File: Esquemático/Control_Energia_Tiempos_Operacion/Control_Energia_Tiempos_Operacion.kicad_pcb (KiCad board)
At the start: 2 copper layers, 100 x 100 mm, 14 parts, among them J1 Conn_01x02_Socket, Q1 BC548, U1 ATmega328P-P, U2 DS3231M, Y1 16MHz

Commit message: Corrección PCB
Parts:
- moved C1 1.52 mm to (146.5, 84.5)
- moved C2 1.52 mm to (141.4, 84.5)
- moved Y1 1.52 mm to (141.6, 91.5)
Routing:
- net Net-(DS1-VO): track 54.5 -> 56.2 mm
- net Net-(U1-XTAL2/PB7): track 16.9 -> 17.7 mm
- net Net-(U1-XTAL1/PB6): track 17.9 -> 17.2 mm
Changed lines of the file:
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@@
   )
   (footprint "Capacitor_THT:C_Disc_D5.0mm_W2.5mm_P2.50mm" (layer "F.Cu")
-    (at 148 84.5 90)
+    (at 146.48 84.5 90)
     (descr "C, Disc series, Radial, pin pitch=2.50mm, , diameter*width=5*2.5mm^2, Capacitor, http://cdn-reichelt.de/documents/datenblatt/B300/DS_KERKO_TC.pdf")
     (tags "C Disc series Radial pin pitch 2.50mm  diameter 5mm width 2.5mm Capacitor")
@@
   )
   (footprint "Capacitor_THT:C_Disc_D5.0mm_W2.5mm_P2.50mm" (layer "F.Cu")
-    (at 142.95 84.5 90)
+    (at 141.43 84.5 90)
     (descr "C, Disc series, Radial, pin pitch=2.50mm, , diameter*width=5*2.5mm^2, Capacitor, http://cdn-reichelt.de/documents/datenblatt/B300/DS_KERKO_TC.pdf")
     (tags "C Disc series Radial pin pitch 2.50mm  diameter 5mm width 2.5mm Capacitor")
@@
   )
   (footprint "Crystal:Crystal_HC49-4H_Vertical" (layer "F.Cu")
-    (at 143.07 91.5)
+    (at 141.55 91.5)
     (descr "Crystal THT HC-49-4H http://5hertz.com/pdfs/04404_D.pdf")
     (tags "THT crystalHC-49-4H")
@@
     (pad "2" thru_hole roundrect (at 0 0) (size 2 2) (drill 1) (layers "*.Cu" "*.Mask") (roundrect_rratio 0.147059)
       (net 2 "+5V") (pinfunction "VDD") (pintype "power_in"))
-    (pad "3" thru_hole circle (at 0 7.62) (size 2 2) (drill 1) (layers "*.Cu" "*.Mask")
+    (pad "3" thru_hole circle (at 0 5.08) (size 2 2) (drill 1) (layers "*.Cu" "*.Mask")
       (net 3 "Net-(DS1-VO)") (pinfunction "VO") (pintype "input"))
     (pad "4" thru_hole circle (at 2.54 0) (size 2 2) (drill 1) (layers "*.Cu" "*.Mask")
       (net 4 "LCD_RS") (pinfunction "RS") (pintype "input"))
-    (pad "5" thru_hole circle (at 0 5.08) (size 2 2) (drill 1) (layers "*.Cu" "*.Mask")
+    (pad "5" thru_hole circle (at 0 7.62) (size 2 2) (drill 1) (layers "*.Cu" "*.Mask")
       (net 1 "GND") (pinfunction "R/W") (pintype "input"))
     (pad "6" thru_hole circle (at 2.54 2.54) (size 2 2) (drill 1) (layers "*.Cu" "*.Mask")
@@
     (pad "1" thru_hole circle (at 2.54 2.54 180) (size 1.7 1.7) (drill 1) (layers "*.Cu" "*.Mask")
       (net 2 "+5V") (pinfunction "V+") (pintype "power_in"))
-    (pad "2" thru_hole circle (at 2.54 0 180) (size 1.7 1.7) (drill 1) (layers "*.Cu" "*.Mask")
+    (pad "2" thru_hole circle (at 2.54 5.08 180) (size 1.7 1.7) (drill 1) (layers "*.Cu" "*.Mask")
       (net 1 "GND") (pinfunction "GND") (pintype "power_in"))
     (pad "3" thru_hole circle (at 0 2.54 180) (size 1.7 1.7) (drill 1) (layers "*.Cu" "*.Mask")
@@
     (pad "5" thru_hole circle (at 0 5.08 180) (size 1.7 1.7) (drill 1) (layers "*.Cu" "*.Mask")
       (net 11 "SWITCH") (pinfunction "SW") (pintype "output"))
-    (pad "6" thru_hole circle (at 2.54 5.08 180) (size 1.7 1.7) (drill 1) (layers "*.Cu" "*.Mask"))
+    (pad "6" thru_hole circle (at 2.54 0 180) (size 1.7 1.7) (drill 1) (layers "*.Cu" "*.Mask"))
     (model "${KICAD6_3DMODEL_DIR}/Connector_IDC.3dshapes/IDC-Header_2x03_P2.54mm_Vertical.wrl"
       (offset (xyz 0 0 0))
@@
   (via (at 189 136) (size 2.5) (drill 1.25) (layers "F.Cu" "B.Cu") (free) (net 1))
   (via (at 147 121) (size 2.5) (drill 1.25) (layers "F.Cu" "B.Cu") (free) (net 1))
-  (segment (start 124 121) (end 124 129) (width 1) (layer "F.Cu") (net 2))
+  (segment (start 124 121) (end 124 132) (width 1) (layer "F.Cu") (net 2))
   (via (at 124 121) (size 2.5) (drill 1.25) (layers "F.Cu" "B.Cu") (free) (net 2))
-  (via (at 124 129) (size 2.5) (drill 1.25) (layers "F.Cu" "B.Cu") (free) (net 2))
-  (segment (start 129 141) (end 129 138) (width 1.5) (layer "B.Cu") (net 2))
+  (via (at 124 132) (size 2.5) (drill 1.25) (layers "F.Cu" "B.Cu") (free) (net 2))
   (segment (start 102 134) (end 102 106) (width 1.5) (layer "B.Cu") (net 2))
   (segment (start 108.46 106.46) (end 102.46 106.46) (width 1.5) (layer "B.Cu") (net 2))
   (segment (start 190 121) (end 194 121) (width 1) (layer "B.Cu") (net 2))
+  (segment (start 129 138) (end 129 141) (width 1.5) (layer "B.Cu") (net 2))
   (segment (start 102 100) (end 102 90) (width 1.5) (layer "B.Cu") (net 2))
-  (segment (start 129 138) (end 124 133) (width 1.5) (layer "B.Cu") (net 2))
   (segment (start 102.46 106.46) (end 102 106) (width 1.5) (layer "B.Cu") (net 2))
-  (segment (start 124 133) (end 124 129) (width 1.5) (layer "B.Cu") (net 2))
   (segment (start 194 132) (end 194 122) (width 1.5) (layer "B.Cu") (net 2))
   (segment (start 194 122) (end 194 121) (width 1.5) (layer "B.Cu") (net 2))
@@
   (segment (start 129 141) (end 129 147) (width 1.5) (layer "B.Cu") (net 2))
   (segment (start 115 147) (end 102 134) (width 1.5) (layer "B.Cu") (net 2))
+  (segment (start 124 133) (end 129 138) (width 1.5) (layer "B.Cu") (net 2))
   (segment (start 153.08 142) (end 153.08 146.92) (width 1.5) (layer "B.Cu") (net 2))
   (segment (start 139 119) (end 139 120) (width 1) (layer "B.Cu") (net 2))
@@
   (segment (start 153 92) (end 187 92) (width 1.5) (layer "B.Cu") (net 2))
   (segment (start 102 88) (end 102 71) (width 1.5) (layer "B.Cu") (net 2))
-  (segment (start 116 145) (end 104 133) (width 1) (layer "B.Cu") (net 3))
-  (segment (start 104 133) (end 104 114.08) (width 1) (layer "B.Cu") (net 3))
+  (segment (start 124 132) (end 124 133) (width 1.5) (layer "B.Cu") (net 2))
+  (segment (start 105.46 111.54) (end 108.46 111.54) (width 1) (layer "B.Cu") (net 3))
   (segment (start 126.46 141) (end 126.46 144.54) (width 1) (layer "B.Cu") (net 3))
   (segment (start 126.46 144.54) (end 126 145) (width 1) (layer "B.Cu") (net 3))
+  (segment (start 104 133) (end 104 113) (width 1) (layer "B.Cu") (net 3))
   (segment (start 126 145) (end 116 145) (width 1) (layer "B.Cu") (net 3))
-  (segment (start 104 114.08) (end 108.46 114.08) (width 1) (layer "B.Cu") (net 3))
+  (segment (start 104 113) (end 105.46 111.54) (width 1) (layer "B.Cu") (net 3))
+  (segment (start 116 145) (end 104 133) (width 1) (layer "B.Cu") (net 3))
   (segment (start 133.985 103.015) (end 118.985 103.015) (width 0.75) (layer "B.Cu") (net 4))
   (segment (start 118.985 103.015) (end 115.54 106.46) (width 0.75) (layer "B.Cu") (net 4))
@@
   (segment (start 140.1 109.9) (end 140.1 108.81) (width 1) (layer "B.Cu") (net 20))
   (segment (start 135 115) (end 140.1 109.9) (width 1) (layer "B.Cu") (net 20))
-  (segment (start 180 111) (end 180 100) (width 1) (layer "F.Cu") (net 21))
-  (via (at 180 111) (size 2.5) (drill 1.25) (layers "F.Cu" "B.Cu") (free) (net 21))
+  (segment (start 180 113) (end 180 100) (width 1) (layer "F.Cu") (net 21))
+  (via (at 180 113) (size 2.5) (drill 1.25) (layers "F.Cu" "B.Cu") (free) (net 21))
   (via (at 180 100) (size 2.5) (drill 1.25) (layers "F.Cu" "B.Cu") (free) (net 21))
-  (segment (start 182 119) (end 190 119) (width 1) (layer "B.Cu") (net 21))
+  (segment (start 180 113) (end 180 117) (width 1) (layer "B.Cu") (net 21))
+  (segment (start 180 117) (end 182 119) (width 1) (layer "B.Cu") (net 21))
   (segment (start 163 99) (end 165 97) (width 1) (layer "B.Cu") (net 21))
   (segment (start 162.96 101.19) (end 162.96 100.84) (width 1) (layer "B.Cu") (net 21))
+  (segment (start 182 119) (end 190 119) (width 1) (layer "B.Cu") (net 21))
   (segment (start 180 99) (end 180 100) (width 1) (layer "B.Cu") (net 21))
-  (segment (start 180 111) (end 180 117) (width 1) (layer "B.Cu") (net 21))
   (segment (start 163 100.8) (end 163 99) (width 1) (layer "B.Cu") (net 21))
   (segment (start 162.96 100.84) (end 163 100.8) (width 1) (layer "B.Cu") (net 21))
   (segment (start 178 97) (end 180 99) (width 1) (layer "B.Cu") (net 21))
   (segment (start 165 97) (end 178 97) (width 1) (layer "B.Cu") (net 21))
-  (segment (start 180 117) (end 182 119) (width 1) (layer "B.Cu") (net 21))
   (segment (start 113.014112 116.62) (end 111 116.62) (width 0.75) (layer "B.Cu") (net 24))
   (segment (start 157.88 108.81) (end 157.88 115.422944) (width 0.75) (layer "B.Cu") (net 24))
@@
   (segment (start 181 108) (end 183 106) (width 1) (layer "B.Cu") (net 27))
   (segment (start 165.5 108.81) (end 166.31 108) (width 1) (layer "B.Cu") (net 27))
-  (segment (start 148 94) (end 148 91.55) (width 1) (layer "B.Cu") (net 30))
-  (segment (start 145.18 96.82) (end 148 94) (width 1) (layer "B.Cu") (net 30))
-  (segment (start 148 91.55) (end 147.95 91.5) (width 1) (layer "B.Cu") (net 30))
-  (segment (start 145.18 101.19) (end 145.18 96.82) (width 1) (layer "B.Cu") (net 30))
-  (segment (start 147.95 84.55) (end 148 84.5) (width 1) (layer "B.Cu") (net 30))
-  (segment (start 147.95 91.5) (end 147.95 84.55) (width 1) (layer "B.Cu") (net 30))
-  (segment (start 143 91.57) (end 143.07 91.5) (width 1) (layer "B.Cu") (net 31))
-  (segment (start 143 100.83) (end 143 91.57) (width 1) (layer "B.Cu") (net 31))
+  (segment (start 146.43 94.57) (end 146.43 91.5) (width 1) (layer "B.Cu") (net 30))
+  (segment (start 145.18 95.82) (end 146.43 94.57) (width 1) (layer "B.Cu") (net 30))
+  (segment (start 146.43 91.5) (end 146.43 84.55) (width 1) (layer "B.Cu") (net 30))
+  (segment (start 146.43 84.55) (end 146.48 84.5) (width 1) (layer "B.Cu") (net 30))
+  (segment (start 145.18 101.19) (end 145.18 95.82) (width 1) (layer "B.Cu") (net 30))
+  (segment (start 141.55 91.5) (end 141.55 84.62) (width 1) (layer "B.Cu") (net 31))
+  (segment (start 142.64 95.64) (end 141.55 94.55) (width 1) (layer "B.Cu") (net 31))
   (segment (start 142.64 101.19) (end 143 100.83) (width 1) (layer "B.Cu") (net 31))
-  (segment (start 143.07 91.5) (end 143.07 84.62) (width 1) (layer "B.Cu") (net 31))
-  (segment (start 143.07 84.62) (end 142.95 84.5) (width 1) (layer "B.Cu") (net 31))
+  (segment (start 142.64 101.19) (end 142.64 95.64) (width 1) (layer "B.Cu") (net 31))
+  (segment (start 141.55 84.62) (end 141.43 84.5) (width 1) (layer "B.Cu") (net 31))
+  (segment (start 141.55 94.55) (end 141.55 91.5) (width 1) (layer "B.Cu") (net 31))
   (segment (start 137 115) (end 142.64 109.36) (width 1) (layer "B.Cu") (net 32))
   (segment (start 142.64 109.36) (end 142.64 108.81) (width 1) (layer "B.Cu") (net 32))

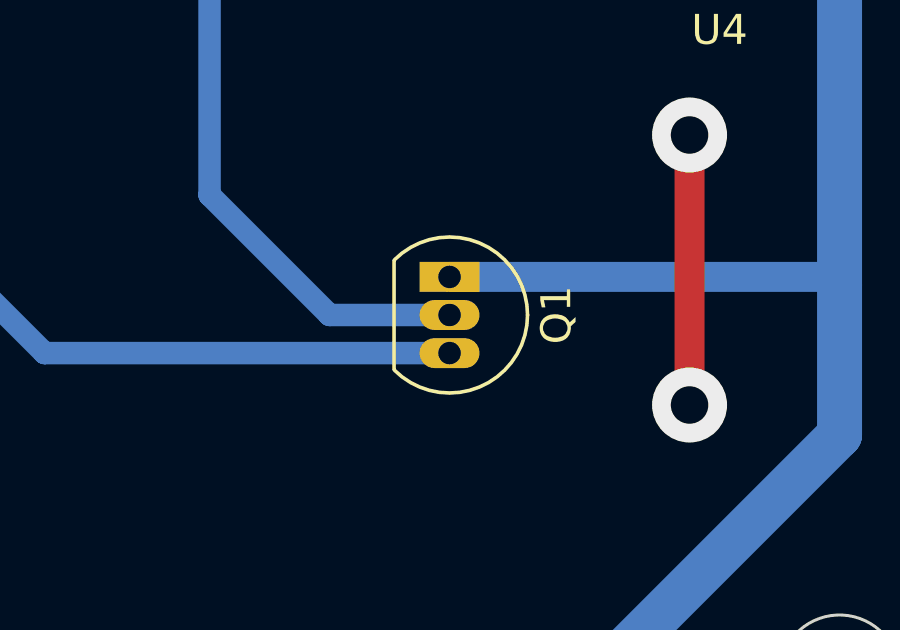
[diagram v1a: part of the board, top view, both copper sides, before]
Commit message: Actualización de PCB, se pueden corregir algunas huellas para el armado de futuros prototipos.
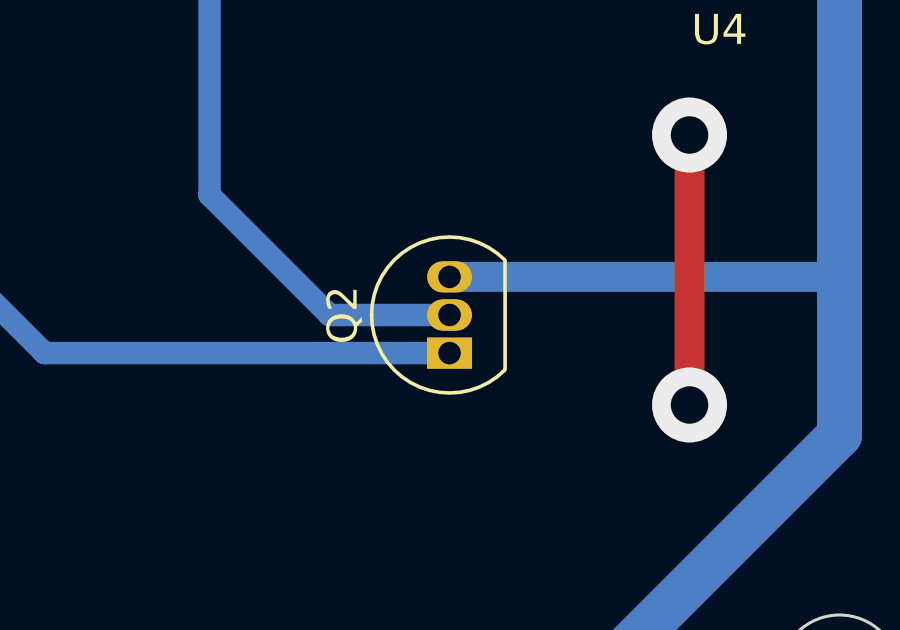
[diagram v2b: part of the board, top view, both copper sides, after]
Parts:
- removed Q1: BC548, Package_TO_SOT_THT:TO-92_Inline
- added Q2: BC558, Package_TO_SOT_THT:TO-92_Inline, F.Cu at (181.0, 134.3)
